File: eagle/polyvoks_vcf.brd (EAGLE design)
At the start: 103.6 x 81 mm, 52 parts, among them IC1 TL072P, IC2 LM4250P, IC3 TL071P, IC4 LM4250P, IC5 TL072P, T1 2N3904

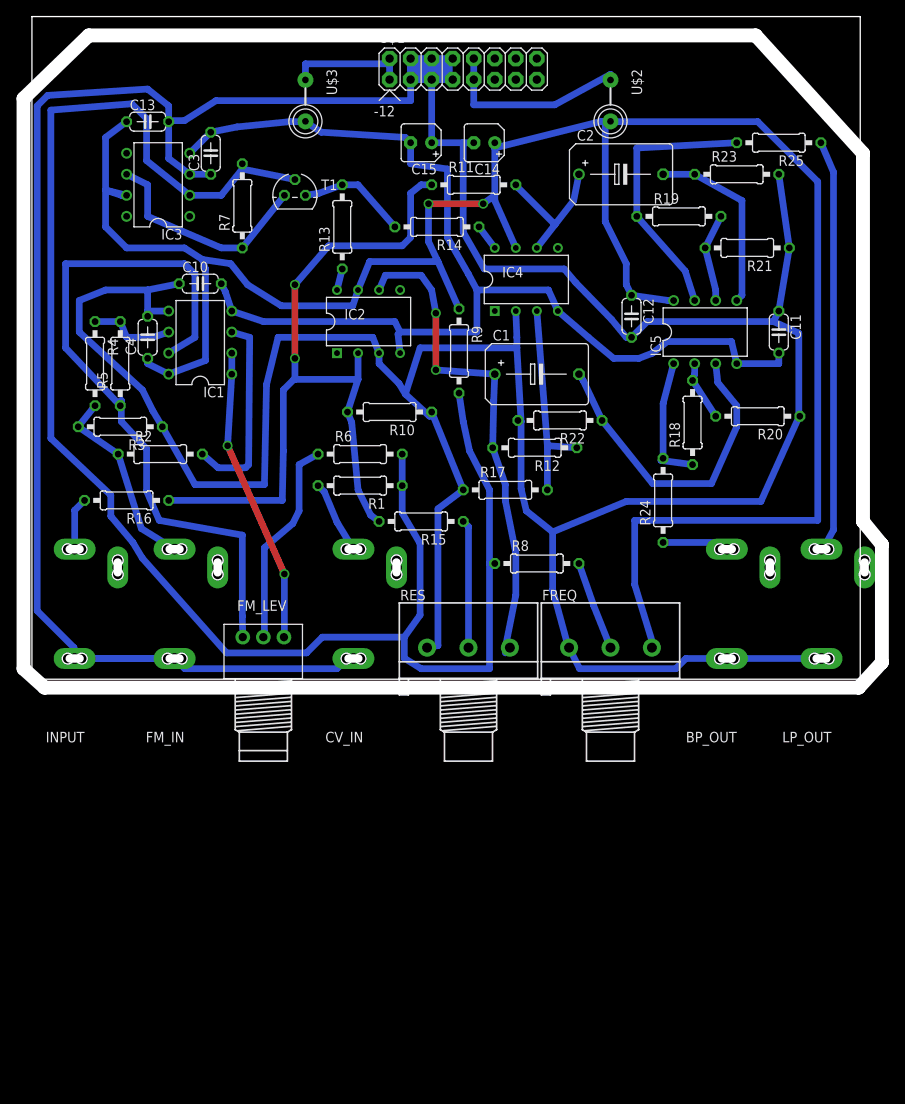
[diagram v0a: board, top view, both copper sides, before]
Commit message: resonance corrected and minified
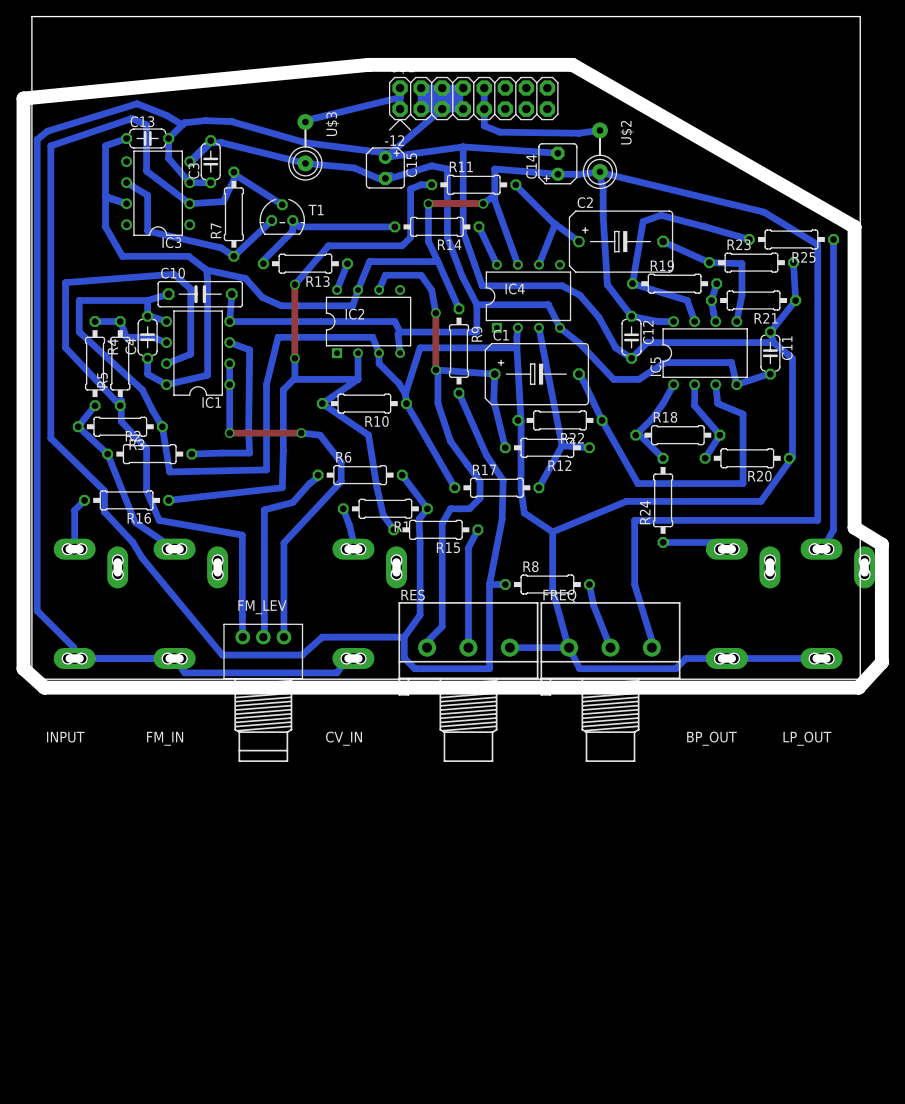
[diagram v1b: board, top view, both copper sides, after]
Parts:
- C10: device rcl:C050-024X044 -> rcl:C075-032X103
- moved R25 11.8 mm to (91.7, 53.1)
- moved R23 10.8 mm to (86.9, 50.3)
- moved C14 9.25 mm to (63.5, 62.2), turned to 90 degrees
- moved R19 8.14 mm to (77.6, 47.8)
- moved C2 8.13 mm to (71.1, 52.8)
- moved R21 6.40 mm to (87.1, 45.7)
- moved R13 6.29 mm to (33.0, 50.2), turned to 180 degrees
- moved U$2 6.23 mm to (68.6, 63.8)
- moved C15 5.29 mm to (42.7, 61.7), turned to 270 degrees
- moved R20 5.24 mm to (86.4, 26.7)
- moved U$3 5.08 mm to (33.0, 64.8)
- moved R1 4.13 mm to (42.7, 20.6)
- moved U$1 3.78 mm to (50.8, 70.1)
- moved T1 3.41 mm to (30.2, 55.4)
- moved R10 3.21 mm to (40.1, 33.3)
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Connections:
- removed net GND: BP_OUT.P$1, C10.1, C11.1, C12.2, C13.2, C14.-, C15.+, C3.1, C4.2, CV_IN.P$1, FM_IN.P$1, FREQ.1, IC1.5, IC2.3, IC3.3, IC4.2, INPUT.P$1, LP_OUT.P$1, R10.1, R17.1, R20.1, R21.1, R22.2, R23.2, R3.1, RES.1, U$1.3, U$1.4, U$1.5, U$1.6, U$1.7, U$1.8
- new net N$30: BP_OUT.P$1, C10.1, C11.1, C12.2, C13.2, C14.-, C15.+, C3.1, C4.2, CV_IN.P$1, FM_IN.P$1, FREQ.1, IC1.5, IC2.3, IC3.3, IC4.2, INPUT.P$1, LP_OUT.P$1, R10.1, R17.1, R20.1, R21.1, R22.2, R23.2, R3.1, RES.3, U$1.3, U$1.4, U$1.5, U$1.6, U$1.7, U$1.8
- net N$13: now also RES.1; no longer RES.3
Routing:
- net GND: track 549.8 -> 0.00 mm
- net N$30: track 0.00 -> 524.8 mm
- net +12V: track 272.6 -> 258.4 mm
- net N$13: track 60.0 -> 73.2 mm
- net N$28: track 50.7 -> 38.7 mm
- net N$2: track 35.8 -> 47.3 mm
- net N$24: track 10.8 -> 4.72 mm
- net N$17: track 13.3 -> 19.3 mm
- net N$23: track 22.7 -> 17.1 mm
- net N$25: track 23.7 -> 18.7 mm
- net N$10: track 94.3 -> 98.8 mm
- net N$5: track 8.85 -> 5.07 mm
- net N$14: track 206.2 -> 202.7 mm
- net N$22: track 7.22 -> 10.5 mm
- net N$29: track 15.8 -> 12.5 mm
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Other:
- outline, holes or cut-outs redrawn

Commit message: schemo modded
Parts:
- added D1, D2: 1N4148DO35-7, diode:DO35-7
- added R26: 47k, rcl:0207/10
- added R27: 100R, rcl:0207/10
- added R28: 470R, rcl:0207/10
- added SOFT_1, SOFT_2: LSP11, solpad:LSP11
- R16: value 47k -> 470k
- R6: value 47k -> 120k
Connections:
- new net GND: R27.2
- new net N$31: R27.1, RES.3
- new net N$32: D1.A, D2.C, R28.1
- new net N$33: D1.C, D2.A, SOFT_1.MP
- net -12V: now also R26.1
- net N$12: now also R28.2
- net N$13: now also SOFT_2.MP
- net N$30: now also R26.2; no longer RES.3
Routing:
- net N$30: track 524.8 -> 517.7 mm
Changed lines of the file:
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@@
 <element name="R14" library="rcl" package="0207/10" value="1M2" x="48.895" y="54.61" rot="R180"/>
 <element name="R15" library="rcl" package="0207/10" value="27k" x="48.768" y="18.034" rot="R180"/>
-<element name="R16" library="rcl" package="0207/10" value="47k" x="11.43" y="21.59" rot="R180"/>
+<element name="R16" library="rcl" package="0207/10" value="470k" x="11.43" y="21.59" rot="R180"/>
 <element name="R17" library="rcl" package="0207/10" value="1k" x="56.134" y="23.114"/>
 <element name="R18" library="rcl" package="0207/10" value="100k" x="77.978" y="29.464"/>
@@
 <element name="R4" library="rcl" package="0207/10" value="100k" x="7.62" y="38.1" rot="R270"/>
 <element name="R5" library="rcl" package="0207/10" value="100k" x="10.668" y="38.1" rot="R90"/>
-<element name="R6" library="rcl" package="0207/10" value="47k" x="39.624" y="24.638"/>
+<element name="R6" library="rcl" package="0207/10" value="120k" x="39.624" y="24.638"/>
 <element name="R7" library="rcl" package="0207/10" value="3k" x="24.384" y="56.134" rot="R90"/>
 <element name="R8" library="rcl" package="0207/10" value="162k" x="62.23" y="11.43"/>
@@
 <element name="U$2" library="adafruit" package="FB" value="FB" x="68.58" y="63.754" rot="R270"/>
 <element name="U$3" library="adafruit" package="FB" value="FB" x="33.02" y="64.77" rot="R270"/>
+<element name="R26" library="rcl" package="0207/10" value="47k" x="5.08" y="-13.97"/>
+<element name="R27" library="rcl" package="0207/10" value="100R" x="5.08" y="-19.05"/>
+<element name="D1" library="diode" package="DO35-7" value="1N4148DO35-7" x="5.08" y="-24.13"/>
+<element name="D2" library="diode" package="DO35-7" value="1N4148DO35-7" x="5.08" y="-30.48"/>
+<element name="R28" library="rcl" package="0207/10" value="470R" x="5.08" y="-38.1"/>
+<element name="SOFT_1" library="solpad" package="LSP11" value="LSP11" x="0" y="-43.18"/>
+<element name="SOFT_2" library="solpad" package="LSP11" value="LSP11" x="0" y="-48.26"/>
 </elements>
 <signals>
@@
 <wire x1="21.59" y1="64.77" x2="22.9" y2="64.77" width="0.8128" layer="16"/>
 <wire x1="22.9" y1="64.77" x2="33.02" y2="62.27" width="0.8128" layer="16"/>
+<contactref element="R26" pad="1"/>
 <wire x1="42.418" y1="60.198" x2="42.672" y2="60.452" width="0" layer="19" extent="16-16"/>
+<wire x1="0" y1="-13.97" x2="23.876" y2="43.18" width="0" layer="19" extent="1-1"/>
 </signal>
 <signal name="N$25">
@@
 <wire x1="52.705" y1="15.875" x2="53.848" y2="18.034" width="0.8128" layer="16"/>
 <wire x1="52.705" y1="3.81" x2="52.705" y2="15.875" width="0.8128" layer="16"/>
+<contactref element="R28" pad="2"/>
+<wire x1="10.16" y1="-38.1" x2="52.705" y2="3.81" width="0" layer="19" extent="1-1"/>
 </signal>
 <signal name="N$13">
@@
 <wire x1="49.022" y1="33.274" x2="49.022" y2="37.084" width="0.8128" layer="16"/>
 <wire x1="49.022" y1="37.084" x2="48.768" y2="37.338" width="0.8128" layer="16"/>
+<contactref element="SOFT_2" pad="MP"/>
+<wire x1="0" y1="-48.26" x2="47.705" y2="3.81" width="0" layer="19" extent="1-1"/>
 </signal>
 <signal name="N$16">
@@
 <wire x1="36.83" y1="0.762" x2="18.455" y2="0.762" width="0.8128" layer="16"/>
 <wire x1="18.455" y1="0.762" x2="17.225" y2="2.5" width="0.8128" layer="16"/>
-<contactref element="RES" pad="3"/>
-<wire x1="57.705" y1="3.81" x2="64.85" y2="3.81" width="0.8128" layer="16"/>
 <wire x1="20.955" y1="67.437" x2="18.415" y2="67.183" width="0.8128" layer="16"/>
 <wire x1="18.415" y1="67.183" x2="18.161" y2="66.929" width="0.8128" layer="16"/>
@@
 <wire x1="16.256" y1="68.072" x2="18.161" y2="66.929" width="0.8128" layer="16"/>
 <wire x1="33.02" y1="64.77" x2="42.926" y2="63.5" width="0.8128" layer="16"/>
+<contactref element="R26" pad="2"/>
 <wire x1="24.257" y1="67.31" x2="24.13" y2="67.31" width="0" layer="19" extent="16-16"/>
 <wire x1="42.672" y1="62.992" x2="42.926" y2="63.5" width="0" layer="19" extent="16-16"/>
 <wire x1="83.9" y1="2.5" x2="78.954" y2="2.5" width="0" layer="19" extent="16-16"/>
+<wire x1="10.16" y1="-13.97" x2="18.455" y2="0.762" width="0" layer="19" extent="16-16"/>
+</signal>
+<signal name="N$31">
+<contactref element="RES" pad="3"/>
+<contactref element="R27" pad="1"/>
+<wire x1="0" y1="-19.05" x2="57.705" y2="3.81" width="0" layer="19" extent="1-1"/>
+</signal>
+<signal name="GND">
+<contactref element="R27" pad="2"/>
+</signal>
+<signal name="N$32">
+<contactref element="R28" pad="1"/>
+<contactref element="D2" pad="C"/>
+<contactref element="D1" pad="A"/>
+<wire x1="1.27" y1="-30.48" x2="0" y2="-38.1" width="0" layer="19" extent="1-1"/>
+<wire x1="8.89" y1="-24.13" x2="1.27" y2="-30.48" width="0" layer="19" extent="1-1"/>
+</signal>
+<signal name="N$33">
+<contactref element="SOFT_1" pad="MP"/>
+<contactref element="D1" pad="C"/>
+<contactref element="D2" pad="A"/>
+<wire x1="8.89" y1="-30.48" x2="0" y2="-43.18" width="0" layer="19" extent="1-1"/>
+<wire x1="1.27" y1="-24.13" x2="8.89" y2="-30.48" width="0" layer="19" extent="1-1"/>
 </signal>
 </signals>

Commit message: mods into layout
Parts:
- moved SOFT_2 91.0 mm to (47.8, 29.2)
- moved SOFT_1 84.9 mm to (44.5, 29.2)
- moved R28 76.5 mm to (47.8, 25.4)
- moved R26 76.5 mm to (72.9, 21.3), turned to 270 degrees
- moved D2 73.9 mm to (41.7, 33.8)
- moved R27 67.6 mm to (62.7, 16.3)
- moved D1 66.6 mm to (41.7, 31.5), turned to 180 degrees
- moved R6 11.1 mm to (29.5, 20.1)
- moved R17 7.55 mm to (61.2, 28.7)
- moved R22 5.08 mm to (63.8, 26.2)
- moved R15 4.68 mm to (47.8, 22.6)
- moved R10 3.82 mm to (39.9, 37.1)
- moved R12 3.70 mm to (61.2, 31.5)
- moved R24 2.54 mm to (78.7, 21.6)
- moved R1 2.40 mm to (41.4, 18.5), turned to 0 degrees
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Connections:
- removed net GND: R27.2
- new net N$34: FREQ.1, R26.2
- net N$30: now also R27.2; no longer FREQ.1, R26.2
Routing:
- net N$34: track 0.00 -> 18.0 mm
- net N$31: track 0.00 -> 15.2 mm
- net N$32: track 0.00 -> 10.2 mm
- net -12V: track 137.0 -> 146.8 mm
- net N$10: track 98.8 -> 89.1 mm
- net N$30: track 517.7 -> 509.8 mm
- net N$16: track 23.6 -> 15.9 mm
- net N$12: track 14.5 -> 21.6 mm
- net N$9: track 23.5 -> 17.9 mm
- net N$2: track 47.3 -> 42.1 mm
- net N$33: track 0.00 -> 4.79 mm
- net +12V: track 258.4 -> 253.8 mm
- net N$21: track 41.7 -> 45.9 mm
- net N$5: track 5.07 -> 8.99 mm
- net N$14: track 202.7 -> 199.7 mm
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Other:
- outline, holes or cut-outs redrawn
